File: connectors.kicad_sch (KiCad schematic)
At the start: 18 parts, among them J2 Screw_Terminal_01x04

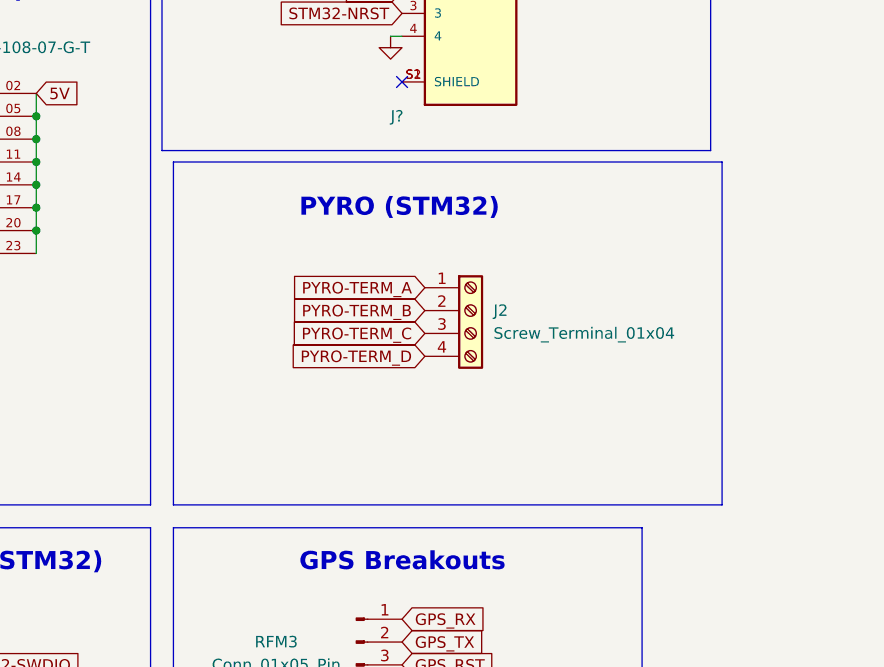
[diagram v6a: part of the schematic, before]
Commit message: added power planes
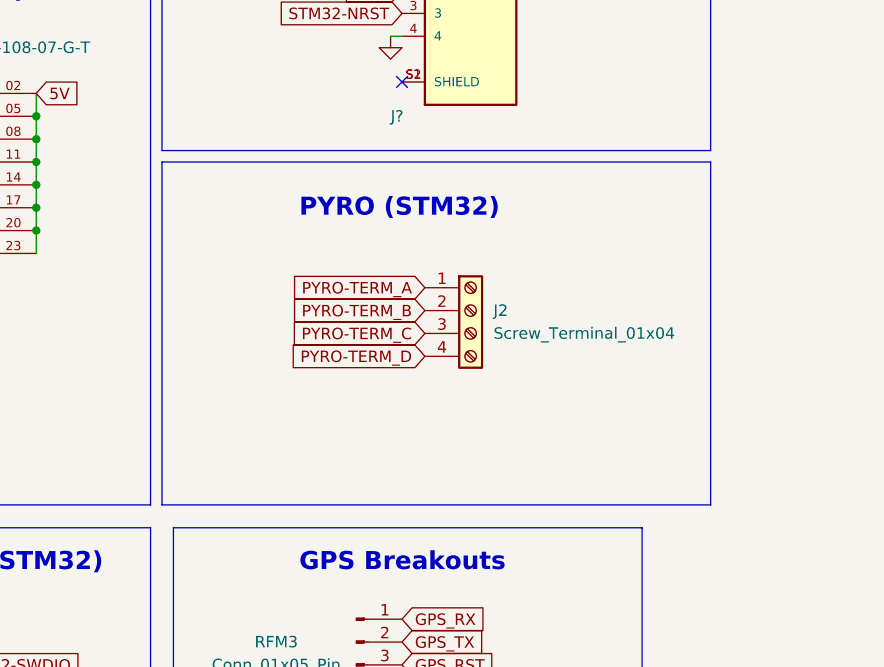
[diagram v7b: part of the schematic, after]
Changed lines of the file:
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@@
     (fill (type none))
   )
-  (rectangle (start 124.46 83.82) (end 185.42 121.92)
+  (rectangle (start 123.19 83.82) (end 184.15 121.92)
     (stroke (width 0) (type default))
     (fill (type none))
